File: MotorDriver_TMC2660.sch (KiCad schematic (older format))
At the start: 17 parts, among them U4 TMC2660

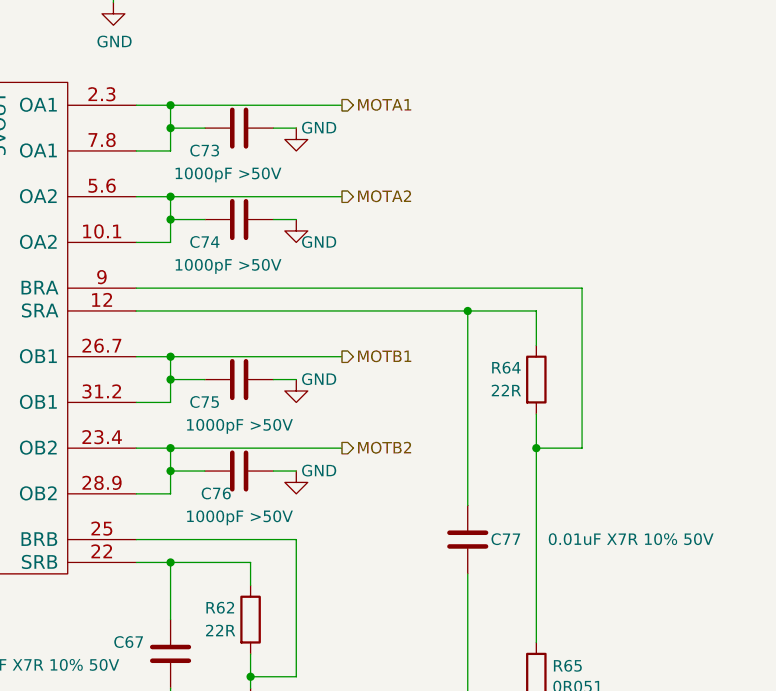
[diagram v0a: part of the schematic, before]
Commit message: Rename some somponents to suite PNP process.
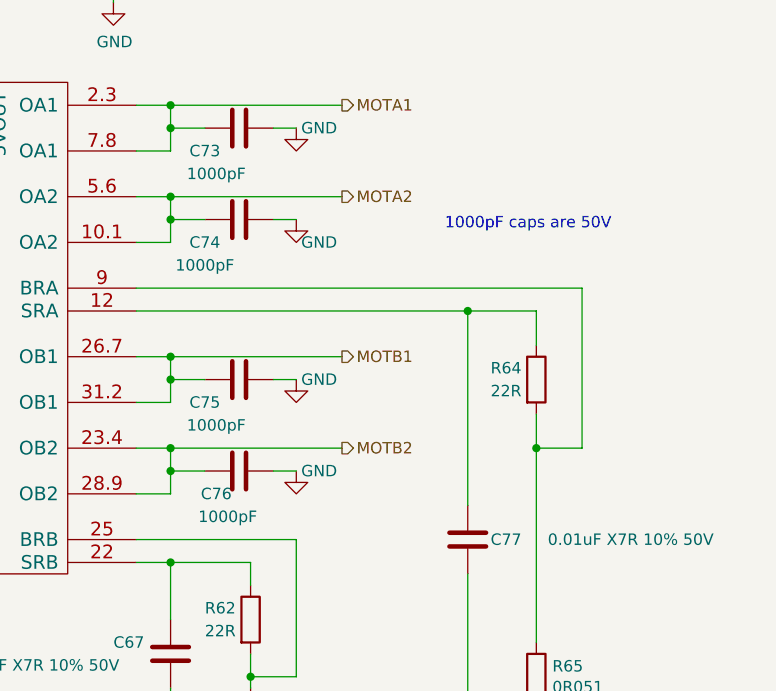
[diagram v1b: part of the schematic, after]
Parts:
- C11, C12, C13, C14: value 1000pF >50V -> 1000pF
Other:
- note added: "1000pF caps are 50V"
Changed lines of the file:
@@
 $Descr A4 11693 8268
 encoding utf-8
-Sheet 17 35
+Sheet 26 35
 Title ""
 Date ""
@@
 AR Path="/5AC337B6/5AD9F95A/5AD4B0F5/5AC33CA1" Ref="C73"  Part="1"
 F 0 "C73" V 6300 2600 50  0000 C CNN
-F 1 "1000pF >50V" V 6400 2700 50  0000 C CNN
+F 1 "1000pF" V 6400 2650 50  0000 C CNN
 F 2 "Capacitor_SMD:C_0603_1608Metric" H 6238 2600 50  0001 C CNN
 F 3 "~" H 6200 2750 50  0001 C CNN
@@
 AR Path="/5AC337B6/5AD9F95A/5AD4B0F5/5AC33D6E" Ref="C74"  Part="1"
 F 0 "C74" V 6300 3000 50  0000 C CNN
-F 1 "1000pF >50V" V 6400 3100 50  0000 C CNN
+F 1 "1000pF" V 6400 3000 50  0000 C CNN
 F 2 "Capacitor_SMD:C_0603_1608Metric" H 6238 3000 50  0001 C CNN
 F 3 "~" H 6200 3150 50  0001 C CNN
@@
 AR Path="/5AC337B6/5AD9F95A/5AD4B0F5/5AC33DC1" Ref="C75"  Part="1"
 F 0 "C75" V 6300 3700 50  0000 C CNN
-F 1 "1000pF >50V" V 6400 3850 50  0000 C CNN
+F 1 "1000pF" V 6400 3750 50  0000 C CNN
 F 2 "Capacitor_SMD:C_0603_1608Metric" H 6238 3700 50  0001 C CNN
 F 3 "~" H 6200 3850 50  0001 C CNN
@@
 AR Path="/5AC337B6/5AD9F95A/5AD4B0F5/5AC33E6E" Ref="C76"  Part="1"
 F 0 "C76" V 6300 4150 50  0000 C CNN
-F 1 "1000pF >50V" V 6400 4250 50  0000 C CNN
+F 1 "1000pF" V 6400 4200 50  0000 C CNN
 F 2 "Capacitor_SMD:C_0603_1608Metric" H 6238 4100 50  0001 C CNN
 F 3 "~" H 6200 4250 50  0001 C CNN
@@
 Wire Wire Line
 	3250 3950 4000 3950
+Text Notes 7100 3200 0    50   ~ 0
+1000pF caps are 50V
 $EndSCHEMATC
